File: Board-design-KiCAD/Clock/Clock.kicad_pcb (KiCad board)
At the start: 2 copper layers, 13 parts, among them M1 SevSeg4Inch, M2 SevSeg4Inch, Y1 SevSeg1.8Inch, Y2 SevSeg1.8Inch, Y3 SevSeg1.8Inch, Y4 SevSeg1.8Inch

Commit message: Nada
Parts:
- removed REF**: BarrelJack_Horizontal, Connector_BarrelJack:BarrelJack_Horizontal
- added PowerSupply: Barrel_Jack_Switch, Connector_BarrelJack:BarrelJack_Horizontal, F.Cu at (-98.8, 28.6)
- added Regulator-11V: LM2596T-ADJ, Package_TO_SOT_THT:TO-220-5_Horizontal_TabUp, F.Cu at (-89.0, 32.0)
- moved H1 4.26 mm to (6.10, 101.6)
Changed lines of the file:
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@@
     (thickness 1.6)
     (drawings 0)
-    (tracks 0)
+    (tracks 1)
     (zones 0)
-    (modules 13)
+    (modules 14)
     (nets 34)
   )
@@
   )
   (module Connector_BarrelJack:BarrelJack_Horizontal (layer F.Cu)
-    (at -54.356 29.464)
+    (at -98.806 28.575)
     (descr "DC Barrel Jack")
     (tags "Power Jack")
-    (fp_text reference REF** (at -8.45 5.75) (layer F.SilkS)
-      (effects (font (size 1 1) (thickness 0.15)))
-    )
-    (fp_text value BarrelJack_Horizontal (at -6.2 -5.5) (layer F.Fab)
+    (fp_text reference PowerSupply (at -8.45 5.75) (layer F.SilkS)
+      (effects (font (size 1 1) (thickness 0.15)))
+    )
+    (fp_text value Barrel_Jack_Switch (at -6.2 -5.5) (layer F.Fab)
       (effects (font (size 1 1) (thickness 0.15)))
     )
@@
     (pad 1 thru_hole rect (at 0 0) (size 3.5 3.5) (drill oval 1 3) (layers *.Cu *.Mask))
     (model ${KISYS3DMOD}/Connector_BarrelJack.3dshapes/BarrelJack_Horizontal.wrl
+      (at (xyz 0 0 0))
+      (scale (xyz 1 1 1))
+      (rotate (xyz 0 0 0))
+    )
+  )
+  (module Package_TO_SOT_THT:TO-220-5_Horizontal_TabUp (layer F.Cu)
+    (at -89 32)
+    (descr "TO-220-5, Horizontal, RM 1.7mm, Pentawatt, Multiwatt-5, see http://www.analog.com/media/en/package-pcb-resources/package/pkg_pdf/ltc-legacy-to-220/to-220_5_05-08-1421_straight_lead.pdf")
+    (tags "TO-220-5 Horizontal RM 1.7mm Pentawatt Multiwatt-5")
+    (fp_text reference Regulator-11V (at 3.4 20.58) (layer F.SilkS)
+      (effects (font (size 1 1) (thickness 0.15)))
+    )
+    (fp_text value LM2596T-ADJ (at 3.4 -1.9) (layer F.Fab)
+      (effects (font (size 1 1) (thickness 0.15)))
+    )
+    (fp_circle (center 3.4 16.66) (end 5.25 16.66) (layer F.Fab) (width 0.1))
+    (fp_line (start -1.6 13.06) (end -1.6 19.46) (layer F.Fab) (width 0.1))
+    (fp_line (start -1.6 19.46) (end 8.4 19.46) (layer F.Fab) (width 0.1))
+    (fp_line (start 8.4 19.46) (end 8.4 13.06) (layer F.Fab) (width 0.1))
+    (fp_line (start 8.4 13.06) (end -1.6 13.06) (layer F.Fab) (width 0.1))
+    (fp_line (start -1.6 3.81) (end -1.6 13.06) (layer F.Fab) (width 0.1))
+    (fp_line (start -1.6 13.06) (end 8.4 13.06) (layer F.Fab) (width 0.1))
+    (fp_line (start 8.4 13.06) (end 8.4 3.81) (layer F.Fab) (width 0.1))
+    (fp_line (start 8.4 3.81) (end -1.6 3.81) (layer F.Fab) (width 0.1))
+    (fp_line (start 0 3.81) (end 0 0) (layer F.Fab) (width 0.1))
+    (fp_line (start 1.7 3.81) (end 1.7 0) (layer F.Fab) (width 0.1))
+    (fp_line (start 3.4 3.81) (end 3.4 0) (layer F.Fab) (width 0.1))
+    (fp_line (start 5.1 3.81) (end 5.1 0) (layer F.Fab) (width 0.1))
+    (fp_line (start 6.8 3.81) (end 6.8 0) (layer F.Fab) (width 0.1))
+    (fp_line (start -1.721 3.69) (end 8.52 3.69) (layer F.SilkS) (width 0.12))
+    (fp_line (start -1.721 13.18) (end 8.52 13.18) (layer F.SilkS) (width 0.12))
+    (fp_line (start -1.721 3.69) (end -1.721 13.18) (layer F.SilkS) (width 0.12))
+    (fp_line (start 8.52 3.69) (end 8.52 13.18) (layer F.SilkS) (width 0.12))
+    (fp_line (start -1.721 19.58) (end -0.521 19.58) (layer F.SilkS) (width 0.12))
+    (fp_line (start 0.68 19.58) (end 1.88 19.58) (layer F.SilkS) (width 0.12))
+    (fp_line (start 3.08 19.58) (end 4.28 19.58) (layer F.SilkS) (width 0.12))
+    (fp_line (start 5.48 19.58) (end 6.68 19.58) (layer F.SilkS) (width 0.12))
+    (fp_line (start 7.88 19.58) (end 8.52 19.58) (layer F.SilkS) (width 0.12))
+    (fp_line (start -1.721 13.42) (end -1.721 14.62) (layer F.SilkS) (width 0.12))
+    (fp_line (start -1.721 15.82) (end -1.721 17.02) (layer F.SilkS) (width 0.12))
+    (fp_line (start -1.721 18.22) (end -1.721 19.42) (layer F.SilkS) (width 0.12))
+    (fp_line (start 8.52 13.42) (end 8.52 14.62) (layer F.SilkS) (width 0.12))
+    (fp_line (start 8.52 15.82) (end 8.52 17.02) (layer F.SilkS) (width 0.12))
+    (fp_line (start 8.52 18.22) (end 8.52 19.42) (layer F.SilkS) (width 0.12))
+    (fp_line (start 0 1.05) (end 0 3.69) (layer F.SilkS) (width 0.12))
+    (fp_line (start 1.7 1.05) (end 1.7 3.69) (layer F.SilkS) (width 0.12))
+    (fp_line (start 3.4 1.05) (end 3.4 3.69) (layer F.SilkS) (width 0.12))
+    (fp_line (start 5.1 1.05) (end 5.1 3.69) (layer F.SilkS) (width 0.12))
+    (fp_line (start 6.8 1.05) (end 6.8 3.69) (layer F.SilkS) (width 0.12))
+    (fp_line (start -1.85 -1.15) (end -1.85 19.71) (layer F.CrtYd) (width 0.05))
+    (fp_line (start -1.85 19.71) (end 8.65 19.71) (layer F.CrtYd) (width 0.05))
+    (fp_line (start 8.65 19.71) (end 8.65 -1.15) (layer F.CrtYd) (width 0.05))
+    (fp_line (start 8.65 -1.15) (end -1.85 -1.15) (layer F.CrtYd) (width 0.05))
+    (pad 5 thru_hole oval (at 6.8 0) (size 1.275 1.8) (drill 1.1) (layers *.Cu *.Mask))
+    (pad 4 thru_hole oval (at 5.1 0) (size 1.275 1.8) (drill 1.1) (layers *.Cu *.Mask))
+    (pad 3 thru_hole oval (at 3.4 0) (size 1.275 1.8) (drill 1.1) (layers *.Cu *.Mask))
+    (pad 2 thru_hole oval (at 1.7 0) (size 1.275 1.8) (drill 1.1) (layers *.Cu *.Mask))
+    (pad 1 thru_hole rect (at 0 0) (size 1.275 1.8) (drill 1.1) (layers *.Cu *.Mask))
+    (pad "" np_thru_hole oval (at 3.4 16.66) (size 3.5 3.5) (drill 3.5) (layers *.Cu *.Mask))
+    (model ${KISYS3DMOD}/Package_TO_SOT_THT.3dshapes/TO-220-5_Horizontal_TabUp.wrl
       (at (xyz 0 0 0))
       (scale (xyz 1 1 1))
@@
   )
   (module Custom:SevSeg4inch (layer F.Cu)
-    (at 10.16 100.33)
+    (at 6.096 101.6)
     (fp_text reference H1 (at 0 0.5) (layer F.SilkS)
       (effects (font (size 1 1) (thickness 0.15)))
@@
     (pad 1 thru_hole rect (at -10.16 12) (size 1.5 1.5) (drill 0.8) (layers *.Cu *.Mask))
   )
+  (segment (start 87.376 155.1) (end 87.376 154.94) (width 0.25) (layer F.Cu) (net 1))
 )

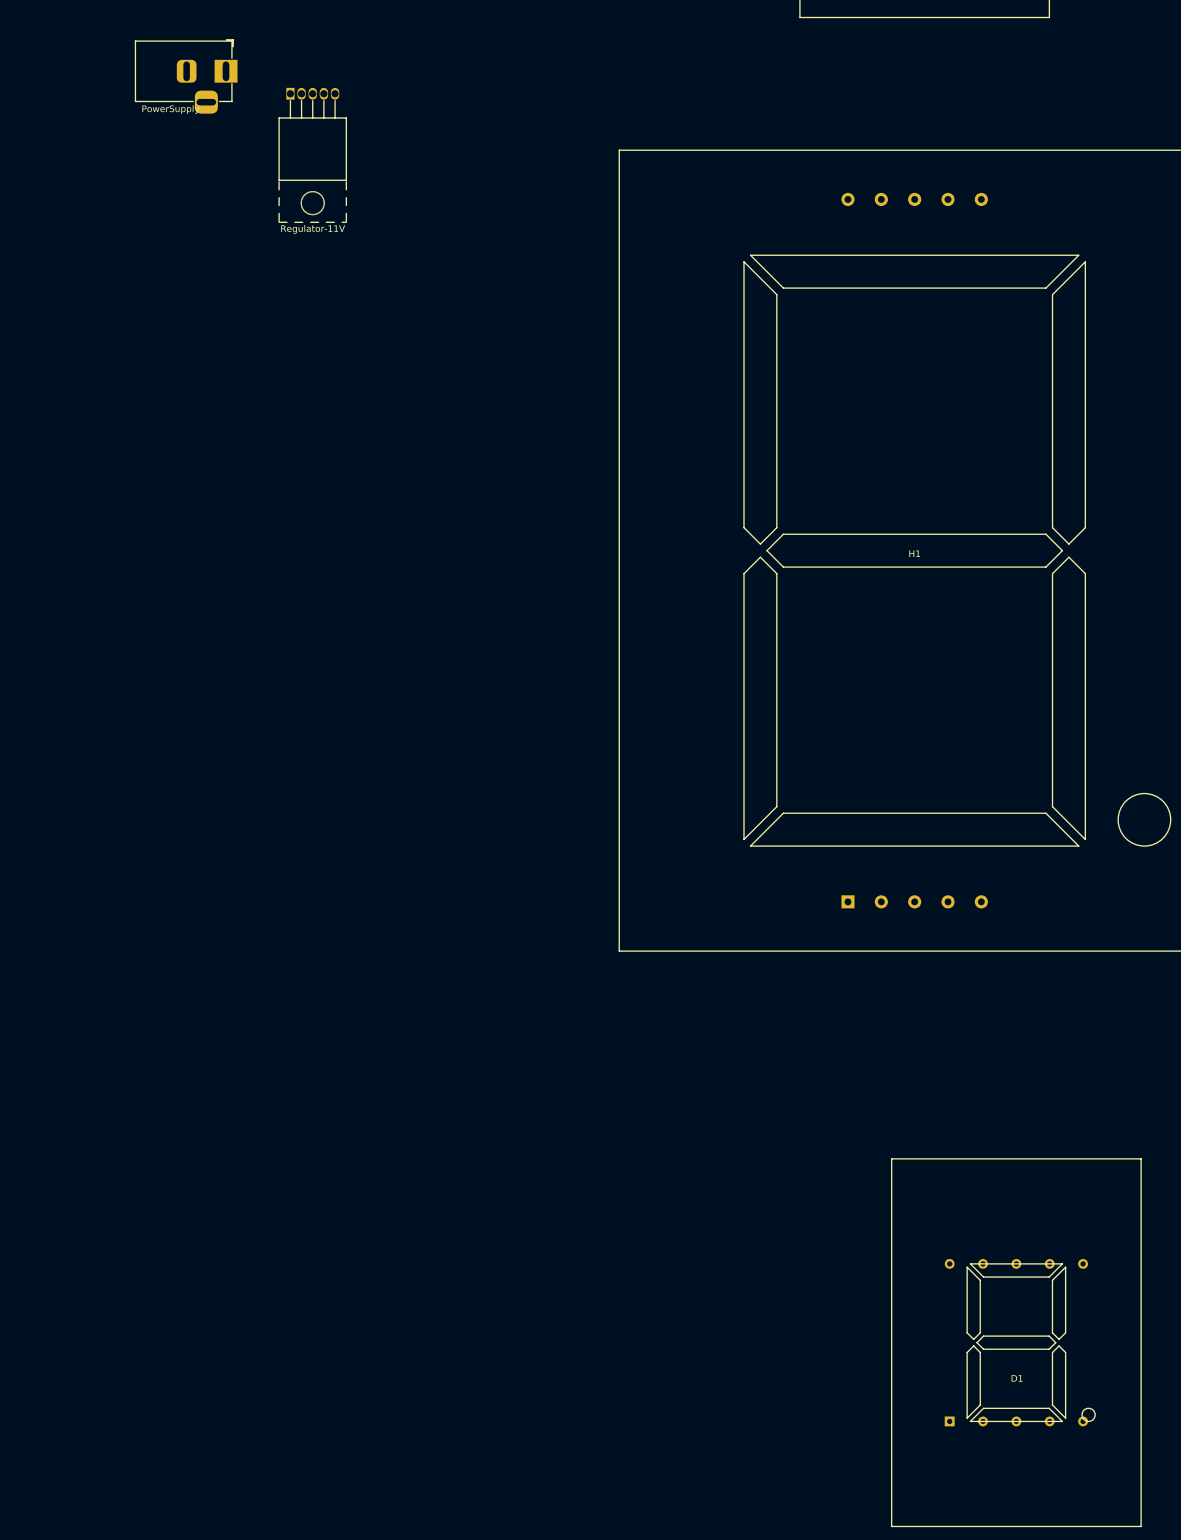
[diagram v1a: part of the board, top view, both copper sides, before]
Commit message: Build PCB part for external power supply
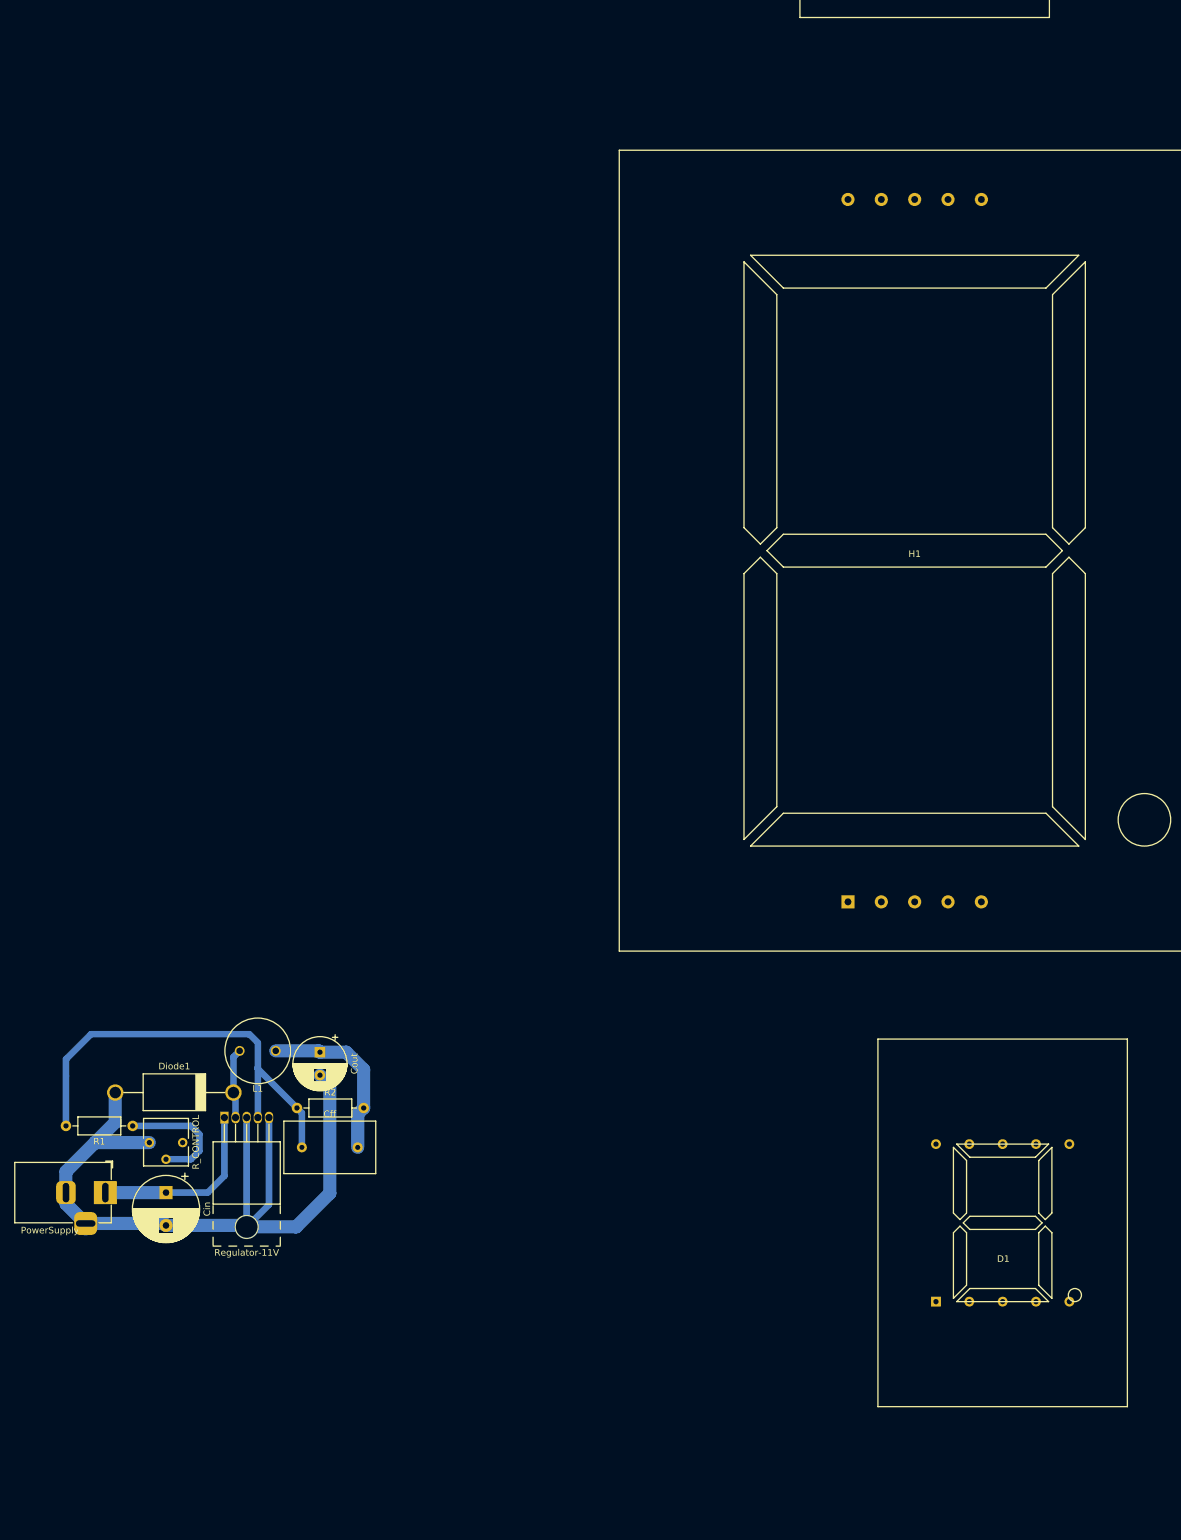
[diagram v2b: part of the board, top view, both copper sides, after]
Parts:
- added Cff: 470pF, Custom:CP_Radial_H15.0mm_W14.0mm_T8.0mm_P8.5mm_Horizontal, F.Cu at (-83.0, 192.5)
- added Cin: 470uF, Capacitor_THT:CP_Radial_D10.0mm_P5.00mm, F.Cu at (-108.0, 199.4)
- added Cout: 100uF, Capacitor_THT:CP_Radial_D8.0mm_P3.50mm, F.Cu at (-84.5, 178.0)
- added Diode1: SR540, Custom:D_5600_9500Metric, F.Cu at (-106.7, 184.2)
- added L1: 68uH, Custom:L_Radial_D10.0mm_P5.5mm, F.Cu at (-94.0, 177.8)
- added R1: 8.2k, Resistor_THT:R_Axial_DIN0207_L6.3mm_D2.5mm_P10.16mm_Horizontal, F.Cu at (-113.0, 189.2)
- added R2: 68k, Resistor_THT:R_Axial_DIN0207_L6.3mm_D2.5mm_P10.16mm_Horizontal, F.Cu at (-88.0, 186.5)
- added R_CONTROL: 1k, Potentiometer_THT:Potentiometer_Vishay_T73YP_Vertical, F.Cu at (-110.5, 191.8)
- moved PowerSupply 171.8 mm to (-117.2, 199.4)
- moved Regulator-11V 156.3 mm to (-99.1, 188.0)
- moved D1 18.4 mm to (19.5, 204.0)
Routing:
- net (no net): track 0.00 -> 305.4 mm

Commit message: Add some PCB routes
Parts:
- removed Cff: 470pF, Custom:CP_Radial_H15.0mm_W14.0mm_T8.0mm_P8.5mm_Horizontal
- removed Cin: 470uF, Capacitor_THT:CP_Radial_D10.0mm_P5.00mm
- removed Cout: 100uF, Capacitor_THT:CP_Radial_D8.0mm_P3.50mm
- removed PowerSupply: Barrel_Jack_Switch, Connector_BarrelJack:BarrelJack_Horizontal
- removed R_CONTROL: 1k, Potentiometer_THT:Potentiometer_Vishay_T73YP_Vertical
- removed Regulator-11V: LM2596T-ADJ, Package_TO_SOT_THT:TO-220-5_Horizontal_TabUp
- added BCD-DATE1: 74LS47, Package_DIP:DIP-18_W7.62mm_LongPads, F.Cu at (321.4, 363.9)
- added BCD-TIME1: 74LS47, Package_DIP:DIP-18_W7.62mm_LongPads, F.Cu at (333.1, 363.9)
- added BCD-YEAR1: 74LS47, Package_DIP:DIP-18_W7.62mm_LongPads, F.Cu at (344.6, 363.9)
- added Cff1: 470pF, Custom:CP_Radial_H15.0mm_W14.0mm_T8.0mm_P8.5mm_Horizontal, F.Cu at (150.5, 323.9)
- added Cin1: 470uF, Capacitor_THT:CP_Radial_D10.0mm_P5.00mm, F.Cu at (122.3, 326.7)
- added CommonPinControl1: ULN2003A, Package_DIP:DIP-18_W7.62mm_LongPads, F.Cu at (362.0, 401.7)
- added Cout1: 100uF, Capacitor_THT:CP_Radial_D8.0mm_P3.50mm, F.Cu at (150.3, 308.6)
- added InputPowerConverter1: ULN2003A, Package_DIP:DIP-18_W7.62mm_LongPads, F.Cu at (373.6, 401.7)
- added PowerSupply1: Barrel_Jack_Switch, Connector_BarrelJack:BarrelJack_Horizontal, F.Cu at (114.0, 327.0)
- added R_CONTROL1: 1k, Potentiometer_THT:Potentiometer_Vishay_T73YP_Vertical, F.Cu at (122.2, 318.6)
- added Regulator-11V1: LM2596T-ADJ, Package_TO_SOT_THT:TO-220-5_Horizontal_TabUp, F.Cu at (133.8, 315.9)
- moved Y1 471.7 mm to (260.8, 390.4)
- moved Y2 445.6 mm to (299.9, 390.4)
- moved Y3 378.2 mm to (339.0, 333.3)
- moved Y4 364.3 mm to (378.2, 333.3)
- moved R2 267.5 mm to (145.3, 317.4)
- moved L1 266.6 mm to (138.2, 308.6)
- moved R1 263.5 mm to (117.4, 317.1)
- moved Diode1 259.8 mm to (121.4, 308.6)
- moved H1 249.8 mm to (240.6, 187.6)
- moved H2 249.8 mm to (332.0, 187.6)
- moved M1 245.1 mm to (423.6, 187.6), turned to 180 degrees
- moved M2 242.0 mm to (515.2, 187.7)
- moved D1 240.0 mm to (221.7, 333.3)
- moved D2 210.6 mm to (221.7, 390.4)
- moved Mo1 142.5 mm to (260.8, 333.3)
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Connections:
- D1 pad 1: (no net) -> Net-(D1-Pad1)
- D1 pad 10: (no net) -> Net-(D1-Pad10)
- D1 pad 2: (no net) -> Net-(D1-Pad2)
- D1 pad 3: (no net) -> Net-(D1-Pad3)
- D1 pad 4: (no net) -> Net-(D1-Pad4)
- D1 pad 5: (no net) -> Net-(D1-Pad1)
- D1 pad 6: (no net) -> Net-(D1-Pad6)
- D1 pad 7: (no net) -> Net-(D1-Pad7)
- D1 pad 8: (no net) -> Net-(D1-Pad8)
- D1 pad 9: (no net) -> Net-(D1-Pad9)
- D2 pad 1: (no net) -> Net-(D2-Pad1)
- D2 pad 10: (no net) -> Net-(D2-Pad10)
- D2 pad 2: (no net) -> Net-(D2-Pad2)
- D2 pad 3: (no net) -> Net-(D2-Pad3)
- D2 pad 4: (no net) -> Net-(D2-Pad4)
- D2 pad 5: (no net) -> Net-(D2-Pad1)
- D2 pad 6: (no net) -> Net-(D2-Pad6)
- D2 pad 7: (no net) -> Net-(D2-Pad7)
- D2 pad 8: (no net) -> Net-(D2-Pad8)
- D2 pad 9: (no net) -> Net-(D2-Pad9)
- Diode1 pad 1: (no net) -> /OUT
- Diode1 pad 2: (no net) -> GND
- H1 pad 1: GND -> Net-(H1-Pad1)
- H1 pad 10: Net-(U1-Pad10) -> /TIME_G
- H1 pad 2: Net-(U1-Pad2) -> /TIME_E
- H1 pad 3: Net-(U1-Pad3) -> /TIME_D
- H1 pad 4: Net-(U1-Pad4) -> /TIME_C
- H1 pad 6: Net-(U1-Pad6) -> /TIME_B
- H1 pad 7: Net-(U1-Pad7) -> /TIME_A
- H1 pad 8: GND -> Net-(H1-Pad1)
- H1 pad 9: Net-(U1-Pad9) -> /TIME_F
- H2 pad 1: GND -> Net-(H2-Pad1)
- H2 pad 10: Net-(U2-Pad10) -> /TIME_G
- H2 pad 2: Net-(U2-Pad2) -> /TIME_E
- H2 pad 3: Net-(U2-Pad3) -> /TIME_D
- H2 pad 4: Net-(U2-Pad4) -> /TIME_C
- H2 pad 6: Net-(U2-Pad6) -> /TIME_B
- H2 pad 7: Net-(U2-Pad7) -> /TIME_A
- H2 pad 8: GND -> Net-(H2-Pad1)
- H2 pad 9: Net-(U2-Pad9) -> /TIME_F
- L1 pad 1: (no net) -> /OUT
- L1 pad 2: (no net) -> +11V
- M1 pad 1: GND -> Net-(M1-Pad1)
- M1 pad 10: Net-(U3-Pad10) -> /TIME_G
- M1 pad 2: Net-(U3-Pad2) -> /TIME_B
- M1 pad 3: Net-(U3-Pad3) -> /TIME_A
- M1 pad 4: Net-(U3-Pad4) -> /TIME_F
- M1 pad 6: Net-(U3-Pad6) -> /TIME_E
- M1 pad 7: Net-(U3-Pad7) -> /TIME_D
- M1 pad 8: GND -> Net-(M1-Pad1)
- M1 pad 9: Net-(U3-Pad9) -> /TIME_C
- M2 pad 1: GND -> Net-(M2-Pad1)
- M2 pad 10: Net-(U4-Pad10) -> /TIME_G
- M2 pad 2: Net-(U4-Pad2) -> /TIME_E
- M2 pad 3: Net-(U4-Pad3) -> /TIME_D
- M2 pad 4: Net-(U4-Pad4) -> /TIME_C
- M2 pad 6: Net-(U4-Pad6) -> /TIME_B
- M2 pad 7: Net-(U4-Pad7) -> /TIME_A
- M2 pad 8: GND -> Net-(M2-Pad1)
- M2 pad 9: Net-(U4-Pad9) -> /TIME_F
- Mo1 pad 1: (no net) -> Net-(Mo1-Pad1)
- Mo1 pad 10: (no net) -> Net-(Mo1-Pad10)
- Mo1 pad 2: (no net) -> Net-(Mo1-Pad2)
- Mo1 pad 3: (no net) -> Net-(Mo1-Pad3)
- Mo1 pad 4: (no net) -> Net-(Mo1-Pad4)
- Mo1 pad 5: (no net) -> Net-(Mo1-Pad1)
- Mo1 pad 6: (no net) -> Net-(Mo1-Pad6)
- Mo1 pad 7: (no net) -> Net-(Mo1-Pad7)
- Mo1 pad 8: (no net) -> Net-(Mo1-Pad8)
- Mo1 pad 9: (no net) -> Net-(Mo1-Pad9)
- Mo2 pad 1: (no net) -> Net-(Mo2-Pad1)
- Mo2 pad 10: (no net) -> Net-(Mo2-Pad10)
- Mo2 pad 2: (no net) -> Net-(Mo2-Pad2)
- Mo2 pad 3: (no net) -> Net-(Mo2-Pad3)
- Mo2 pad 4: (no net) -> Net-(Mo2-Pad4)
- Mo2 pad 5: (no net) -> Net-(Mo2-Pad1)
- Mo2 pad 6: (no net) -> Net-(Mo2-Pad6)
- Mo2 pad 7: (no net) -> Net-(Mo2-Pad7)
- Mo2 pad 8: (no net) -> Net-(Mo2-Pad8)
- Mo2 pad 9: (no net) -> Net-(Mo2-Pad9)
- R1 pad 1: (no net) -> Net-(R1-Pad1)
- R1 pad 2: (no net) -> /FEEDBACK
- R2 pad 1: (no net) -> /FEEDBACK
- R2 pad 2: (no net) -> +11V
- Y1 pad 1: (no net) -> Net-(Y1-Pad1)
- Y1 pad 10: (no net) -> Net-(Y1-Pad10)
- Y1 pad 2: (no net) -> Net-(Y1-Pad2)
- Y1 pad 3: (no net) -> Net-(Y1-Pad3)
- Y1 pad 4: (no net) -> Net-(Y1-Pad4)
- Y1 pad 5: (no net) -> Net-(Y1-Pad1)
- Y1 pad 6: (no net) -> Net-(Y1-Pad6)
- Y1 pad 7: (no net) -> Net-(Y1-Pad7)
- Y1 pad 8: (no net) -> Net-(Y1-Pad8)
- Y1 pad 9: (no net) -> Net-(Y1-Pad9)
- Y2 pad 1: (no net) -> Net-(Y2-Pad1)
- Y2 pad 10: (no net) -> Net-(Y2-Pad10)
- Y2 pad 2: (no net) -> Net-(Y2-Pad2)
- Y2 pad 3: (no net) -> Net-(Y2-Pad3)
- Y2 pad 4: (no net) -> Net-(Y2-Pad4)
- Y2 pad 5: (no net) -> Net-(Y2-Pad1)
- Y2 pad 6: (no net) -> Net-(Y2-Pad6)
- Y2 pad 7: (no net) -> Net-(Y2-Pad7)
- Y2 pad 8: (no net) -> Net-(Y2-Pad8)
- Y2 pad 9: (no net) -> Net-(Y2-Pad9)
- Y3 pad 1: (no net) -> Net-(Y3-Pad1)
- Y3 pad 10: (no net) -> Net-(Y3-Pad10)
- Y3 pad 2: (no net) -> Net-(Y3-Pad2)
- Y3 pad 3: (no net) -> Net-(Y3-Pad3)
- Y3 pad 4: (no net) -> Net-(Y3-Pad4)
- Y3 pad 5: (no net) -> Net-(Y3-Pad1)
- Y3 pad 6: (no net) -> Net-(Y3-Pad6)
- Y3 pad 7: (no net) -> Net-(Y3-Pad7)
- Y3 pad 8: (no net) -> Net-(Y3-Pad8)
- Y3 pad 9: (no net) -> Net-(Y3-Pad9)
- Y4 pad 1: (no net) -> Net-(Y4-Pad1)
- Y4 pad 10: (no net) -> Net-(Y4-Pad10)
- Y4 pad 2: (no net) -> Net-(Y4-Pad2)
- Y4 pad 3: (no net) -> Net-(Y4-Pad3)
- Y4 pad 4: (no net) -> Net-(Y4-Pad4)
- Y4 pad 5: (no net) -> Net-(Y4-Pad1)
- Y4 pad 6: (no net) -> Net-(Y4-Pad6)
- Y4 pad 7: (no net) -> Net-(Y4-Pad7)
- Y4 pad 8: (no net) -> Net-(Y4-Pad8)
- Y4 pad 9: (no net) -> Net-(Y4-Pad9)
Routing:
- net /TIME_G: track 0.00 -> 883.6 mm
- net /TIME_A: track 0.00 -> 400.4 mm
- net /TIME_F: track 0.00 -> 388.0 mm
- net /TIME_B: track 0.00 -> 362.6 mm
- net (no net): track 305.4 -> 0.00 mm
- net GND: track 0.16 -> 120.2 mm
- net /FEEDBACK: track 0.00 -> 70.4 mm
- net +11V: track 0.00 -> 28.6 mm
- net /+15V: track 0.00 -> 28.2 mm
- net Net-(R1-Pad1): track 0.00 -> 24.8 mm
- net /OUT: track 0.00 -> 12.3 mm
